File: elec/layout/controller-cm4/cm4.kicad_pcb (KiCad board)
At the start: 4 copper layers, 10 parts

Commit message: update ethernet layout
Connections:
- net cm4-line-12 renamed cm4-pins[40]
- net cm4-line-9 renamed cm4-pins[29]
- net cm4.hdi_b-pins[26] renamed pins[26]
- net cm4.hdi_b-pins[38] renamed pins[38]
- net pins[23] renamed cm4.hdi_b-pins[23]
- net pins[28] renamed cm4.hdi_b-pins[28]
- net pins[29] renamed cm4.hdi_b-pins[29]
- net pins[33] renamed cm4.hdi_b-pins[33]
- net pins[40] renamed cm4.hdi_b-pins[40]
- net pins[49] renamed cm4.hdi_b-pins[49]
- CN1 pad 1: (no net) -> GND
- CN1 pad 100: (no net) -> GND
- CN1 pad 11: (no net) -> GND
- CN1 pad 12: cm4-line-7 -> cm4-pins[23]
- CN1 pad 16: (no net) -> GND
- CN1 pad 17: cm4-line-1 -> cm4-pins[33]
- CN1 pad 21: (no net) -> GND
- CN1 pad 22: pins[43] -> cm4-line-8
- CN1 pad 24: pins[47] -> cm4-line-3
- CN1 pad 25: cm4-line -> cm4-pins[49]
- CN1 pad 26: (no net) -> GND
- CN1 pad 27: cm4-line-2 -> pins[53]
- CN1 pad 29: cm4-line-4 -> pins[57]
- CN1 pad 30: (no net) -> GND
- CN1 pad 33: (no net) -> GND
- CN1 pad 37: (no net) -> GND
- CN1 pad 4: (no net) -> GND
- CN1 pad 49: (no net) -> GND
- CN1 pad 65: (no net) -> GND
- CN1 pad 68: (no net) -> GND
- CN1 pad 7: (no net) -> GND
- CN1 pad 71: (no net) -> GND
- CN1 pad 74: (no net) -> GND
- CN1 pad 75: cm4-line-3 -> cm4-line-4
- CN1 pad 77: cm4-line-10 -> cm4-line-2
- CN1 pad 79: (no net) -> GND
- CN1 pad 81: cm4-pins[38] -> cm4-line-6
- CN1 pad 82: cm4-line-11 -> cm4-line-7
- CN1 pad 84: (no net) -> GND
- CN1 pad 85: cm4-line-6 -> cm4-line-1
- CN1 pad 86: cm4-line-8 -> cm4-pins[28]
- CN1 pad 87: cm4-pins[26] -> cm4-line
- CN1 pad 89: (no net) -> GND
- CN1 pad 90: (no net) -> GND
- CN1 pad 94: (no net) -> GND
- CN1 pad 97: (no net) -> GND
- CN2 pad 10: (no net) -> GND
- CN2 pad 13: (no net) -> GND
- CN2 pad 16: (no net) -> GND
- CN2 pad 19: (no net) -> GND
- CN2 pad 22: (no net) -> GND
- CN2 pad 28: (no net) -> GND
- CN2 pad 31: (no net) -> GND
- CN2 pad 34: (no net) -> GND
- CN2 pad 37: (no net) -> GND
- CN2 pad 4: (no net) -> GND
- CN2 pad 40: (no net) -> GND
- CN2 pad 43: (no net) -> GND
- CN2 pad 46: (no net) -> GND
- CN2 pad 49: (no net) -> GND
- CN2 pad 52: (no net) -> GND
- CN2 pad 55: (no net) -> GND
- CN2 pad 58: (no net) -> GND
- CN2 pad 61: (no net) -> GND
- CN2 pad 64: (no net) -> GND
- CN2 pad 67: (no net) -> GND
- CN2 pad 7: (no net) -> GND
- CN2 pad 70: (no net) -> GND
- CN2 pad 73: (no net) -> GND
- CN2 pad 82: (no net) -> GND
- CN2 pad 85: (no net) -> GND
- CN2 pad 88: (no net) -> GND
- CN2 pad 91: (no net) -> GND
- CN2 pad 94: (no net) -> GND
- CN2 pad 97: (no net) -> GND
- D1 pad 1: cm4-cathode-1 -> cm4-cathode
- D2 pad 1: cm4-cathode -> cm4-cathode-1
- R1 pad 1: cm4-cathode-1 -> cm4-cathode
- R2 pad 1: cm4-cathode -> cm4-cathode-1
- RJ1 pad P1: rj45.connector-net-1 -> rj45.connector-net
- RJ1 pad P10: rj45.connector-net -> rj45.connector-net-1
- U1 pad 3: GND -> (no net)

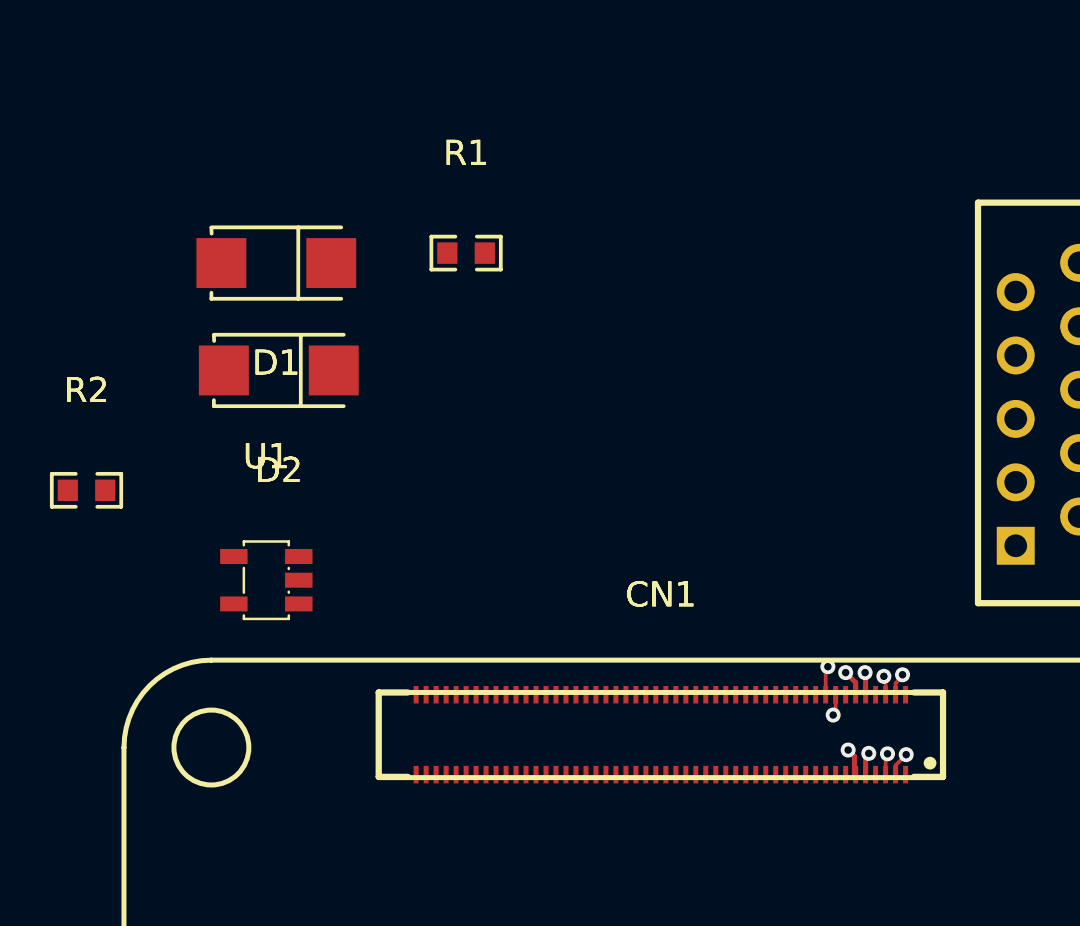
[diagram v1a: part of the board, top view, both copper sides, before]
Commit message: add CAN communication block and RPI CM4 block
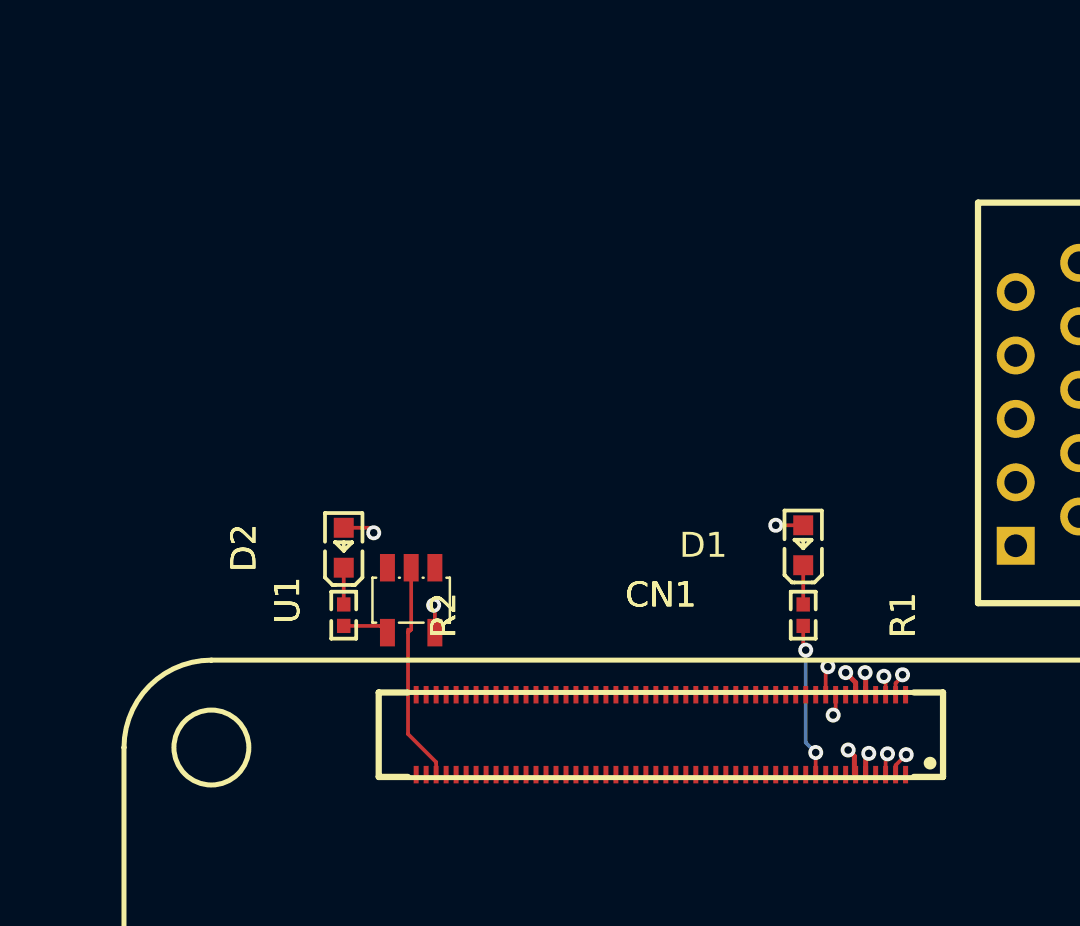
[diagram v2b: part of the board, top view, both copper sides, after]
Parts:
- D1: value infV -> (none); footprint atopile:SMA_L4.3-W2.6-LS5.2-RD-e14692 -> atopile:LED0603-RD-YELLOW-5af84a
- D2: value infV -> (none); footprint atopile:SMA_L4.3-W2.6-LS5.2-RD-e14692 -> atopile:LED0603-RD-c81ffb
- R1, R2: value 10kΩ ±1% 100mW -> 1kΩ ±1% 62.5mW; footprint atopile:R0603-ebcab9 -> atopile:R0402-56259e
- moved D1 23.9 mm to (155.6, 95.7), turned to 90 degrees
- moved R1 19.8 mm to (155.6, 98.5), turned to -90 degrees
- moved R2 11.4 mm to (137.2, 98.5), turned to -90 degrees
- moved D2 7.56 mm to (137.2, 95.8), turned to 90 degrees
- moved U1 5.85 mm to (139.9, 97.9), turned to 90 degrees
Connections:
- net cm4-line-7 renamed line-5
- net cm4-pins[29] renamed line-2
- net cm4-pins[33] renamed line-3
- net cm4.hdi_b-pins[23] renamed pins[23]
- net cm4.hdi_b-pins[28] renamed pins[28]
- net cm4.hdi_b-pins[29] renamed pins[29]
- net cm4.hdi_b-pins[33] renamed pins[33]
- net cm4.hdi_b-pins[39] renamed pins[39]
- net cm4.hdi_b-pins[49] renamed pins[49]
- net pins[26] renamed cm4.hdi_b-pins[26]
- net pins[46] renamed cm4-pins[46]
- net pins[53] renamed line
- net pins[55] renamed line-1
- net pins[57] renamed line-4
- CN1 pad 1: GND -> (no net)
- CN1 pad 100: GND -> (no net)
- CN1 pad 11: GND -> (no net)
- CN1 pad 12: cm4-pins[23] -> cm4-line-5
- CN1 pad 16: GND -> (no net)
- CN1 pad 20: cm4-pins[39] -> cm4-line-1
- CN1 pad 21: GND -> (no net)
- CN1 pad 22: cm4-line-8 -> cm4-line-6
- CN1 pad 24: cm4-line-3 -> cm4-line-2
- CN1 pad 25: cm4-pins[49] -> cm4-line-3
- CN1 pad 26: GND -> (no net)
- CN1 pad 30: GND -> (no net)
- CN1 pad 33: GND -> (no net)
- CN1 pad 37: GND -> (no net)
- CN1 pad 4: GND -> (no net)
- CN1 pad 49: GND -> (no net)
- CN1 pad 65: GND -> (no net)
- CN1 pad 68: GND -> (no net)
- CN1 pad 7: GND -> (no net)
- CN1 pad 71: GND -> (no net)
- CN1 pad 74: GND -> (no net)
- CN1 pad 75: cm4-line-4 -> pins[50]
- CN1 pad 77: cm4-line-2 -> cm4-pins[46]-1
- CN1 pad 78: cm4-line-5 -> cm4-line
- CN1 pad 79: GND -> (no net)
- CN1 pad 81: cm4-line-6 -> line-6
- CN1 pad 84: GND -> (no net)
- CN1 pad 85: cm4-line-1 -> pins[30]
- CN1 pad 86: cm4-pins[28] -> cm4-line-4
- CN1 pad 87: cm4-line -> cm4-pins[26]
- CN1 pad 89: GND -> (no net)
- CN1 pad 90: GND -> (no net)
- CN1 pad 94: GND -> (no net)
- CN1 pad 97: GND -> (no net)
- CN2 pad 10: GND -> (no net)
- CN2 pad 13: GND -> (no net)
- CN2 pad 16: GND -> (no net)
- CN2 pad 19: GND -> (no net)
- CN2 pad 22: GND -> (no net)
- CN2 pad 28: GND -> (no net)
- CN2 pad 31: GND -> (no net)
- CN2 pad 34: GND -> (no net)
- CN2 pad 37: GND -> (no net)
- CN2 pad 4: GND -> (no net)
- CN2 pad 40: GND -> (no net)
- CN2 pad 43: GND -> (no net)
- CN2 pad 46: GND -> (no net)
- CN2 pad 49: GND -> (no net)
- CN2 pad 52: GND -> (no net)
- CN2 pad 55: GND -> (no net)
- CN2 pad 58: GND -> (no net)
- CN2 pad 61: GND -> (no net)
- CN2 pad 64: GND -> (no net)
- CN2 pad 67: GND -> (no net)
- CN2 pad 7: GND -> (no net)
- CN2 pad 70: GND -> (no net)
- CN2 pad 73: GND -> (no net)
- CN2 pad 82: GND -> (no net)
- CN2 pad 85: GND -> (no net)
- CN2 pad 88: GND -> (no net)
- CN2 pad 91: GND -> (no net)
- CN2 pad 94: GND -> (no net)
- CN2 pad 97: GND -> (no net)
- D1 pad 1: cm4-cathode -> cm4-cathode-1
- D2 pad 1: cm4-cathode-1 -> cm4-cathode
- R1 pad 1: cm4-cathode -> cm4-cathode-1
- R2 pad 1: cm4-cathode-1 -> cm4-cathode
- RJ1 pad P1: rj45.connector-net -> rj45.connector-net-1
- RJ1 pad P10: rj45.connector-net-1 -> rj45.connector-net
- U1 pad 3: (no net) -> GND
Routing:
- net PWR_LED: track 0.00 -> 8.93 mm
- net pins[19]: track 0.00 -> 6.16 mm, vias 0 -> 2
- net VCC_3V3: track 0.00 -> 3.50 mm, vias 0 -> 3
- net Y: track 0.00 -> 1.86 mm
- net cm4-cathode-1: track 0.00 -> 1.57 mm
- net cm4-cathode: track 0.00 -> 1.47 mm

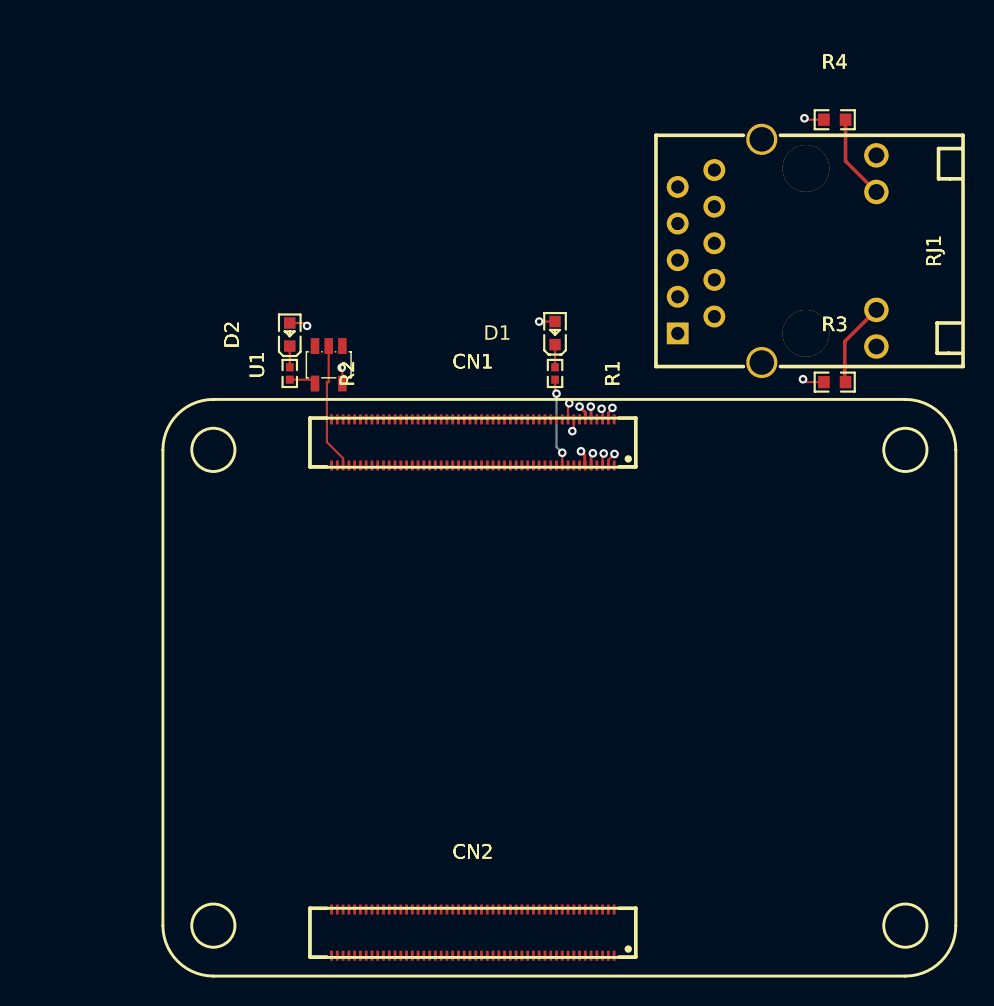
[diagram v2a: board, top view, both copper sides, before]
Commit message: add CAN isolator, cellsim cell
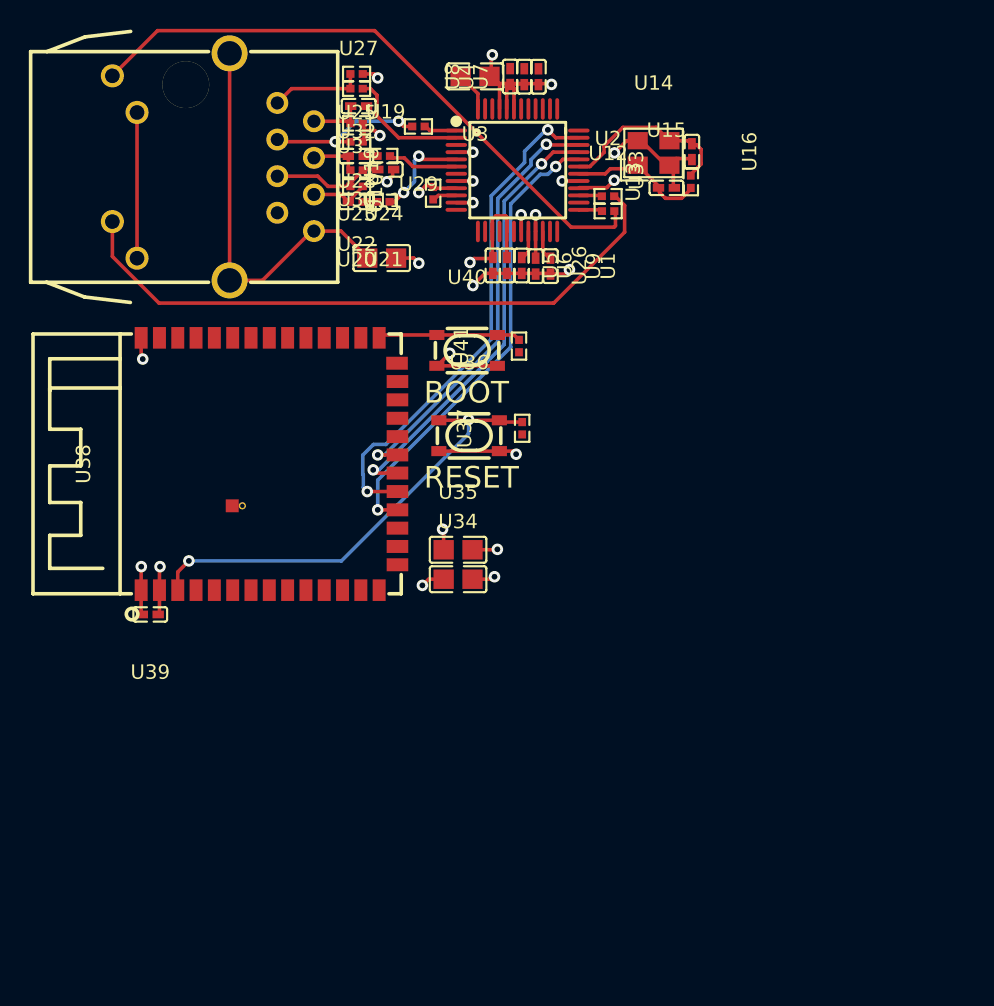
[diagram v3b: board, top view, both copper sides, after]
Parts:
- removed CN1, CN2: , atopile:CONN-SMD_DF40C-100DS-0.4V-51-ceffa9
- removed D1: , atopile:LED0603-RD-YELLOW-5af84a
- removed D2: , atopile:LED0603-RD-c81ffb
- removed R1, R2: 1kΩ ±1% 62.5mW, atopile:R0402-56259e
- removed R3, R4: 470Ω ±1% 100mW, atopile:R0603-ebcab9
- removed RJ1: , atopile:RJ45-TH_HR911130A-5845d4
- added U10: 12.4kΩ ±1% 62.5mW, atopile:R0402-56259e, F.Cu at (147.1, 86.0)
- added U11: 1nF ±10% 50V X7R, atopile:C0805-3b2e55, F.Cu at (143.6, 90.5)
- added U12: 220Ω ±1% 62.5mW, atopile:R0402-56259e, F.Cu at (159.3, 87.2)
- added U13: 1MΩ ±1% 62.5mW, atopile:R0402-56259e, F.Cu at (165.0, 85.2)
- added U14: , lib:CRYSTAL-SMD_4P-L3.2-W2.5-BL, F.Cu at (162.4, 83.2)
- added U15: 10pF ±5% 50V C0G, atopile:C0402-b3ef17, F.Cu at (163.3, 85.6)
- added U16: 10pF ±5% 50V C0G, atopile:C0402-b3ef17, F.Cu at (165.1, 83.1)
- added U18: , lib:RJ45-TH_J1B1211CCD, F.Cu at (131.9, 84.2)
- added U19: 10nF ±10% 50V X7R, atopile:C0402-b3ef17, F.Cu at (143.9, 84.4)
- added U2: 220Ω ±1% 62.5mW, atopile:R0402-56259e, F.Cu at (159.3, 86.2)
- added U20: 6.8nF ±10% 50V X7R, atopile:C0402-b3ef17, F.Cu at (141.8, 86.6)
- added U21: 33Ω ±1% 62.5mW, atopile:R0402-56259e, F.Cu at (143.7, 86.6)
- added U22: 49.9Ω ±1% 62.5mW, atopile:R0402-56259e, F.Cu at (141.8, 85.5)
- added U23: 6.8nF ±10% 50V X7R, atopile:C0402-b3ef17, F.Cu at (141.8, 83.4)
- added U24: 33Ω ±1% 62.5mW, atopile:R0402-56259e, F.Cu at (143.7, 83.4)
- added U25: 49.9Ω ±1% 62.5mW, atopile:R0402-56259e, F.Cu at (141.8, 84.4)
- added U26: 4.7µF ±10% 10V X5R, atopile:C0402-b3ef17, F.Cu at (153.3, 91.0)
- added U27: 22nF ±10% 50V X7R, atopile:C0402-b3ef17, F.Cu at (142.0, 80.0)
- added U28: 10Ω ±1% 62.5mW, atopile:R0402-56259e, F.Cu at (141.8, 81.2)
- added U29: 33Ω ±1% 62.5mW, atopile:R0402-56259e, F.Cu at (146.1, 81.4)
- added U3: 10µF ±10% 25V X5R, atopile:C0805-3b2e55, F.Cu at (150.1, 77.9)
- added U30: 49.9Ω ±1% 62.5mW, atopile:R0402-56259e, F.Cu at (141.8, 82.4)
- added U31: 33Ω ±1% 62.5mW, atopile:R0402-56259e, F.Cu at (141.8, 78.7)
- added U32: 49.9Ω ±1% 62.5mW, atopile:R0402-56259e, F.Cu at (141.8, 77.7)
- added U33: , lib:LQFP-48_L7.0-W7.0-P0.50-LS9.0-BL, F.Cu at (153.0, 84.4)
- added U34: 10µF ±10% 25V X5R, atopile:C0805-3b2e55, F.Cu at (148.9, 112.8)
- added U35: 10µF ±10% 25V X5R, atopile:C0805-3b2e55, F.Cu at (148.9, 110.7)
- added U36: , lib:KEY-SMD_4P-L4.2-W3.2-P2.20-LS4.6, F.Cu at (149.6, 102.8)
- added U37: 10kΩ ±1% 62.5mW, atopile:R0402-56259e, F.Cu at (153.3, 102.3)
- added U38: , lib:WIRELM-SMD_ESP32-S3-WROOM-1, F.Cu at (135.8, 104.8)
- added U39: 100nF ±10% 16V X7R, atopile:C0402-b3ef17, F.Cu at (127.5, 115.2)
- added U4: 100nF ±10% 16V X7R, atopile:C0402-b3ef17, F.Cu at (153.5, 77.9)
- added U40: , lib:KEY-SMD_4P-L4.2-W3.2-P2.20-LS4.6, F.Cu at (149.5, 96.9)
- added U41: 10kΩ ±1% 62.5mW, atopile:R0402-56259e, F.Cu at (153.1, 96.6)
- added U5: 100nF ±10% 16V X7R, atopile:C0402-b3ef17, F.Cu at (151.3, 91.0)
- added U6: 100nF ±10% 16V X7R, atopile:C0402-b3ef17, F.Cu at (152.3, 91.0)
- added U7: 100nF ±10% 16V X7R, atopile:C0402-b3ef17, F.Cu at (154.5, 77.9)
- added U8: 100nF ±10% 16V X7R, atopile:C0402-b3ef17, F.Cu at (152.5, 77.9)
- added U9: 100nF ±10% 16V X7R, atopile:C0402-b3ef17, F.Cu at (154.3, 91.1)
- U1: value (none) -> 10nF ±10% 50V X7R; footprint atopile:SOT-23-5_L3.0-W1.7-P0.95-LS2.8-BR-9d80aa -> atopile:C0402-b3ef17
- moved U1 16.8 mm to (155.3, 91.1), turned to -90 degrees
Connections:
- U1 pad 1: N_C_ -> _1V2O
- U1 pad 2: PWR_LED -> gnd
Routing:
- net hv: track 2.92 -> 51.9 mm, vias 2 -> 13
- net gnd: track 0.00 -> 45.3 mm, vias 0 -> 14
- net RLED_minus: track 0.00 -> 44.2 mm
- net LLED_minus: track 0.00 -> 42.9 mm
- net mosi: track 0.00 -> 35.6 mm, vias 0 -> 2
- net cs: track 0.00 -> 32.4 mm, vias 0 -> 2
- net in-1: track 0.00 -> 32.2 mm, vias 0 -> 2
- net ETH_LED_ACTIVITY: track 32.0 -> 0.00 mm, vias 1 -> 0
- net sck: track 0.00 -> 31.0 mm, vias 0 -> 2
- net miso: track 0.00 -> 30.3 mm, vias 0 -> 2
- net CGND: track 0.00 -> 27.5 mm
- net ETH_LED_LINK: track 27.0 -> 0.00 mm, vias 1 -> 0
- net ETH_P0_N: track 21.0 -> 0.00 mm, vias 1 -> 0
- net ETH_P3_P: track 19.4 -> 0.00 mm, vias 1 -> 0
- net ETH_P1_N: track 19.2 -> 0.00 mm, vias 1 -> 0
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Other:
- copper layers 4 -> 2
- board text added: "BOOT"
- board text added: "RESET"
